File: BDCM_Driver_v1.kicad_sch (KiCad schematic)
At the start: 37 parts, among them J1 OUT_{A}, J2 Encoder, J3 ST-Link, J4 Power, J5 I^{2}C, J6 Encoder, J7 OUT_{B}, SW1 RST, U1 STM32C011F4Px, U2 TB67H450FNG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

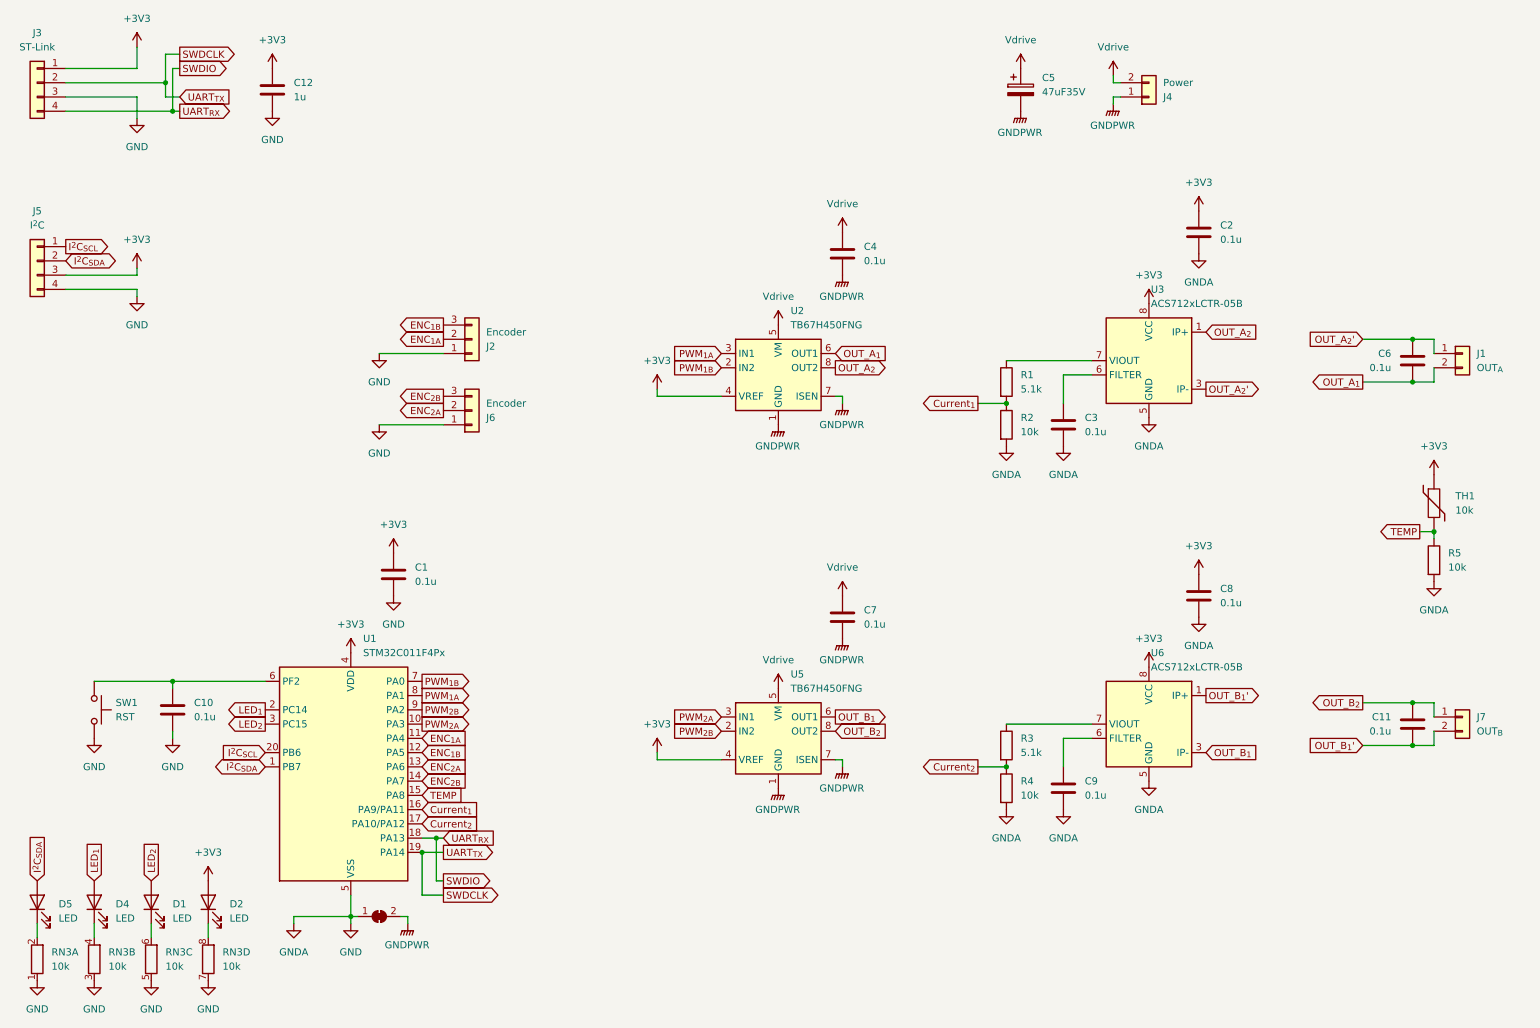
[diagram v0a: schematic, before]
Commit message: ver2.0, change driver IC
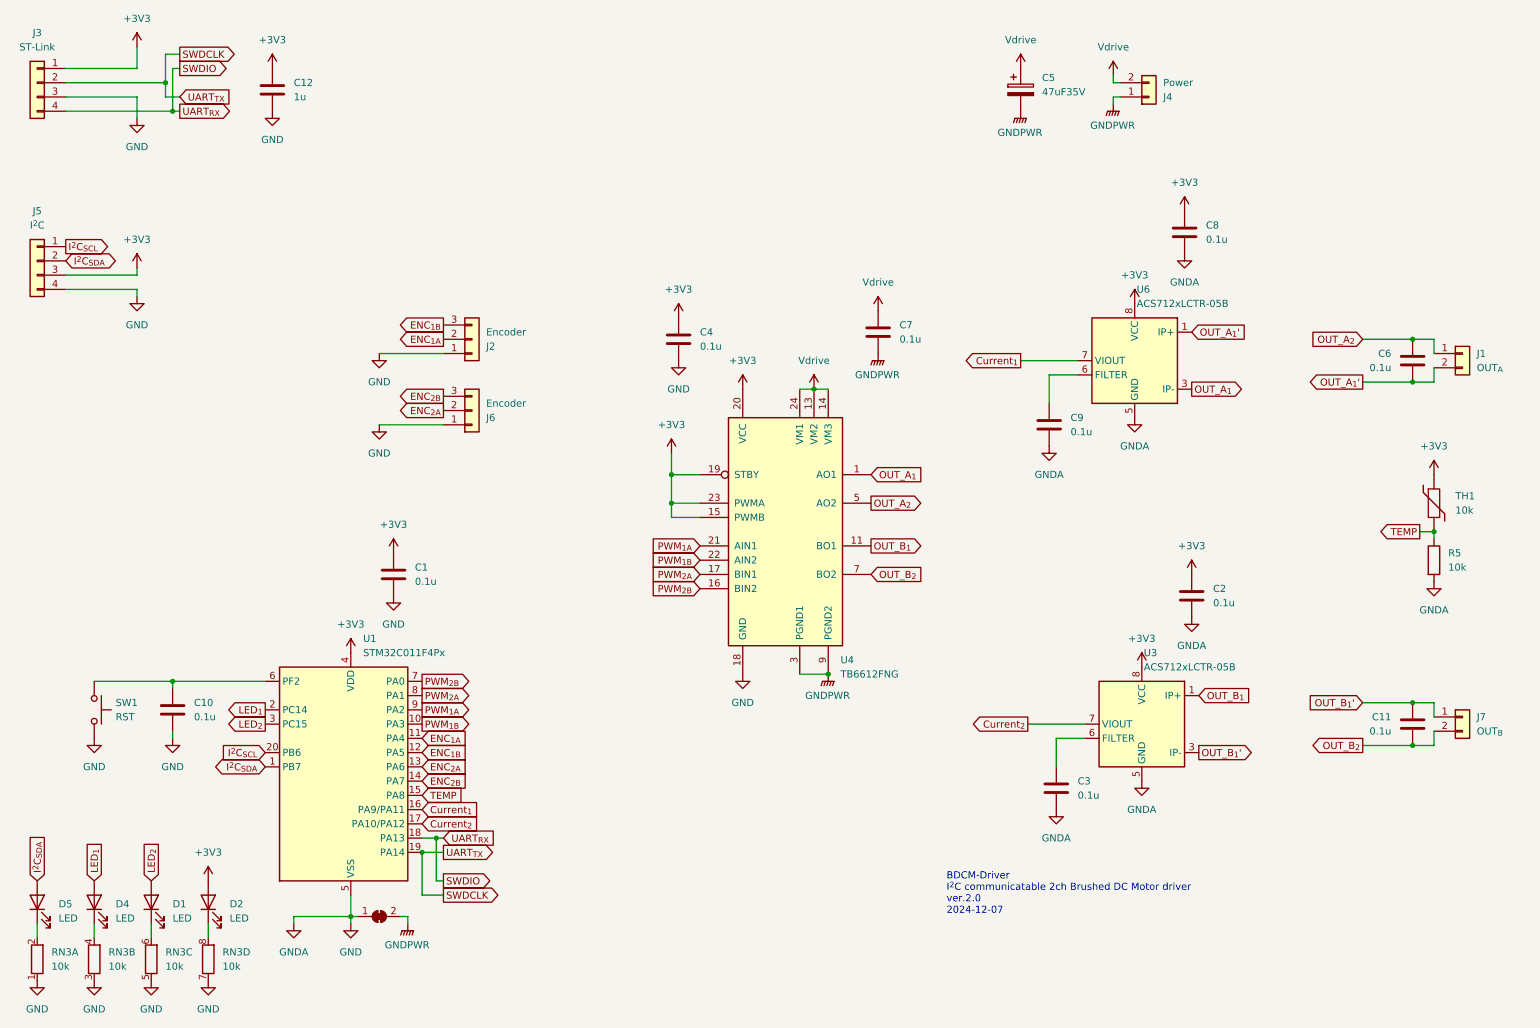
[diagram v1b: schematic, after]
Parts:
- removed R1, R3: 5.1k, Resistor_SMD:R_0603_1608Metric, symbol Device:R
- removed R2, R4: 10k, Resistor_SMD:R_0603_1608Metric, symbol Device:R
- removed U2, U5: TB67H450FNG, Package_SO:Texas_HTSOP-8-1EP_3.9x4.9mm_P1.27mm_EP2.95x4.9mm_Mask2.4x3.1mm_ThermalVias, symbol Driver_Motor:DRV8870DDA
- added U4: TB6612FNG, Package_SO:SSOP-24_5.3x8.2mm_P0.65mm, symbol Driver_Motor:TB6612FNG
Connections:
- net +3V3: now also C4.1, U4.15 (PWMB), U4.19 (STBY), U4.20 (VCC), U4.23 (PWMA)
- net Current_{1}: now also U6.7 (VIOUT)
- net Current_{2}: now also U3.7 (VIOUT)
- net GND: now also C4.2, U4.18 (GND)
- net GNDPWR: now also U4.10 (PGND2), U4.3 (PGND1), U4.4 (PGND1), U4.9 (PGND2); no longer C4.2
- net OUT_A_{1}: now also U6.3 (IP-), U6.4 (IP-), U4.1 (AO1), U4.2 (AO1); no longer C6.2, J1.2 (Pin_2)
- net OUT_A_{2}: now also C6.1, J1.1 (Pin_1), U4.5 (AO2), U4.6 (AO2); no longer U3.1 (IP+), U3.2 (IP+)
- net OUT_B_{1}: now also U3.1 (IP+), U3.2 (IP+), U4.11 (BO1), U4.12 (BO1); no longer U6.3 (IP-), U6.4 (IP-)
- net OUT_B_{1}': now also C11.1, J7.1 (Pin_1), U3.3 (IP-), U3.4 (IP-); no longer C11.2, J7.2 (Pin_2), U6.1 (IP+), U6.2 (IP+)
- net OUT_B_{2}: now also C11.2, J7.2 (Pin_2), U4.7 (BO2), U4.8 (BO2); no longer C11.1, J7.1 (Pin_1)
- net PWM_{1A}: now also U1.9 (PA2), U4.21 (AIN1); no longer U1.8 (PA1)
- net PWM_{1B}: now also U1.10 (PA3), U4.22 (AIN2); no longer U1.7 (PA0)
- net PWM_{2A}: now also U1.8 (PA1), U4.17 (BIN1); no longer U1.10 (PA3)
- net PWM_{2B}: now also U1.7 (PA0), U4.16 (BIN2); no longer U1.9 (PA2)
- net Vdrive: now also U4.13 (VM2), U4.14 (VM3), U4.24 (VM1); no longer C4.1
- removed net OUT_A_{2}': C6.1, J1.1 (Pin_1), U3.3 (IP-), U3.4 (IP-)
- new net OUT_A_{1}': C6.2, J1.2 (Pin_2), U6.1 (IP+), U6.2 (IP+)
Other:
- note added: "BDCM-Driver I^{2}C communicatable 2ch Brushed DC Motor driver ver.2.0 2024-12-07"
- moved on the sheet: C2, C3, C4, C7, C8, C9, U3, U6

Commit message: v2 manifactured
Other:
- moved on the sheet: C6
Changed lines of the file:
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@@
 	)
 	(junction
-		(at 261.62 72.39)
+		(at 261.62 80.01)
 		(diameter 0)
 		(color 0 0 0 0)
@@
 	)
 	(junction
-		(at 261.62 80.01)
+		(at 261.62 72.39)
 		(diameter 0)
 		(color 0 0 0 0)
@@
 	(wire
 		(pts
-			(xy 265.43 74.93) (xy 265.43 72.39)
+			(xy 265.43 77.47) (xy 265.43 80.01)
 		)
 		(stroke
@@
 	(wire
 		(pts
-			(xy 261.62 72.39) (xy 252.73 72.39)
+			(xy 261.62 80.01) (xy 252.73 80.01)
 		)
 		(stroke
@@
 	(wire
 		(pts
-			(xy 261.62 80.01) (xy 265.43 80.01)
+			(xy 261.62 72.39) (xy 265.43 72.39)
 		)
 		(stroke
@@
 	(wire
 		(pts
-			(xy 265.43 80.01) (xy 265.43 77.47)
+			(xy 265.43 72.39) (xy 265.43 74.93)
 		)
 		(stroke
@@
 	(wire
 		(pts
-			(xy 252.73 80.01) (xy 261.62 80.01)
+			(xy 252.73 72.39) (xy 261.62 72.39)
 		)
 		(stroke
@@
 	(wire
 		(pts
-			(xy 265.43 72.39) (xy 261.62 72.39)
+			(xy 265.43 80.01) (xy 261.62 80.01)
 		)
 		(stroke
@@
 	(global_label "OUT_A_{2}"
 		(shape input)
-		(at 252.73 72.39 180)
+		(at 252.73 80.01 180)
 		(fields_autoplaced yes)
 		(effects
@@
 		)
 		(property "Intersheetrefs" "${INTERSHEET_REFS}"
-			(at 243.0416 72.39 0)
+			(at 243.0416 80.01 0)
 			(effects
 				(font
@@
 	(global_label "OUT_A_{1}'"
 		(shape output)
-		(at 252.73 80.01 180)
+		(at 252.73 72.39 180)
 		(fields_autoplaced yes)
 		(effects
@@
 		)
 		(property "Intersheetrefs" "${INTERSHEET_REFS}"
-			(at 242.4876 80.01 0)
+			(at 242.4876 72.39 0)
 			(effects
 				(font
@@
 	(symbol
 		(lib_id "Connector_Generic:Conn_01x02")
-		(at 270.51 74.93 0)
+		(at 270.51 77.47 0)
+		(mirror x)
 		(unit 1)
 		(exclude_from_sim no)
@@
 		(fields_autoplaced yes)
 		(property "Reference" "J1"
-			(at 273.05 74.93 0)
+			(at 273.05 77.47 0)
 			(effects
 				(font
@@
 		)
 		(property "Value" "OUT_{A}"
-			(at 273.05 77.47 0)
+			(at 273.05 74.93 0)
 			(effects
 				(font
@@
 		)
 		(property "Footprint" "Connector_PinHeader_2.54mm:PinHeader_1x02_P2.54mm_Horizontal"
-			(at 270.51 74.93 0)
+			(at 270.51 77.47 0)
 			(effects
 				(font
@@
 		)
 		(property "Datasheet" "~"
-			(at 270.51 74.93 0)
+			(at 270.51 77.47 0)
 			(effects
 				(font
@@
 		)
 		(property "Description" ""
-			(at 270.51 74.93 0)
+			(at 270.51 77.47 0)
 			(effects
 				(font
@@
 	(symbol
 		(lib_id "Device:C")
-		(at 261.62 76.2 0)
-		(mirror y)
+		(at 261.62 76.2 180)
 		(unit 1)
 		(exclude_from_sim no)
@@
 		(dnp no)
 		(property "Reference" "C6"
-			(at 257.81 74.93 0)
+			(at 257.81 77.47 0)
 			(effects
 				(font
@@
 		)
 		(property "Value" "0.1u"
-			(at 257.81 77.47 0)
+			(at 257.81 74.93 0)
 			(effects
 				(font
@@
 		)
 		(property "Footprint" "Capacitor_SMD:C_0603_1608Metric"
-			(at 260.6548 80.01 0)
+			(at 260.6548 72.39 0)
 			(effects
 				(font
